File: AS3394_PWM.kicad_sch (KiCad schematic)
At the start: 90 parts, among them U4 LM324, U5 AS3394, U6 LM324

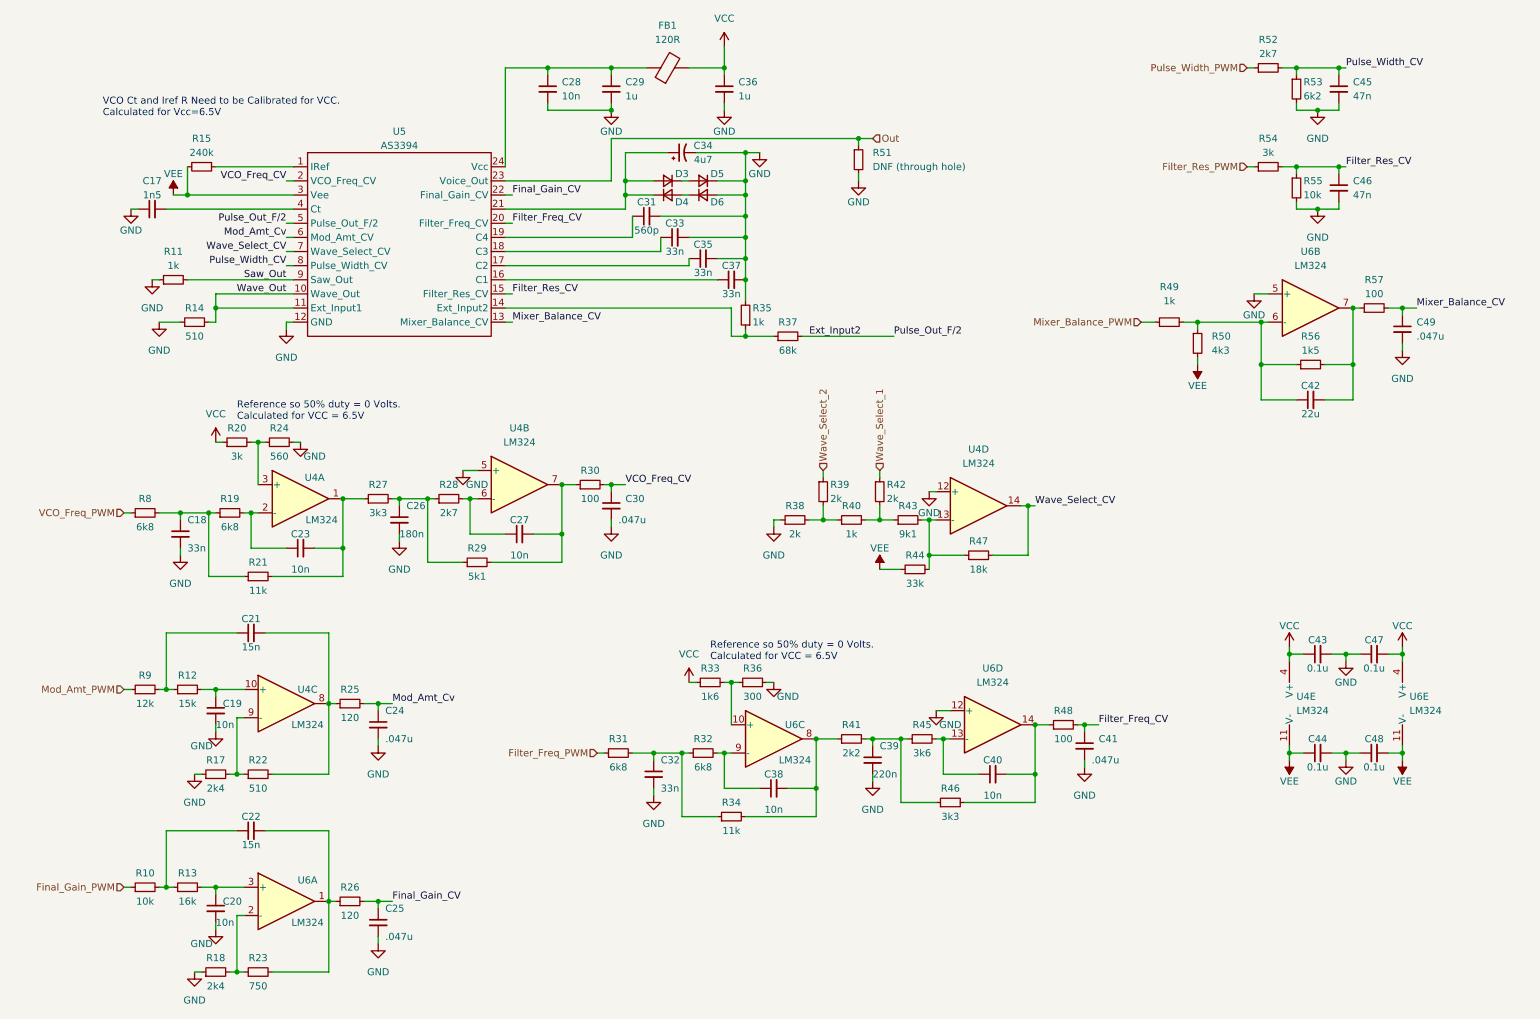
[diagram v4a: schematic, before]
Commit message: Finished most of routing; added TL071 for headphone out; working on adding I/O
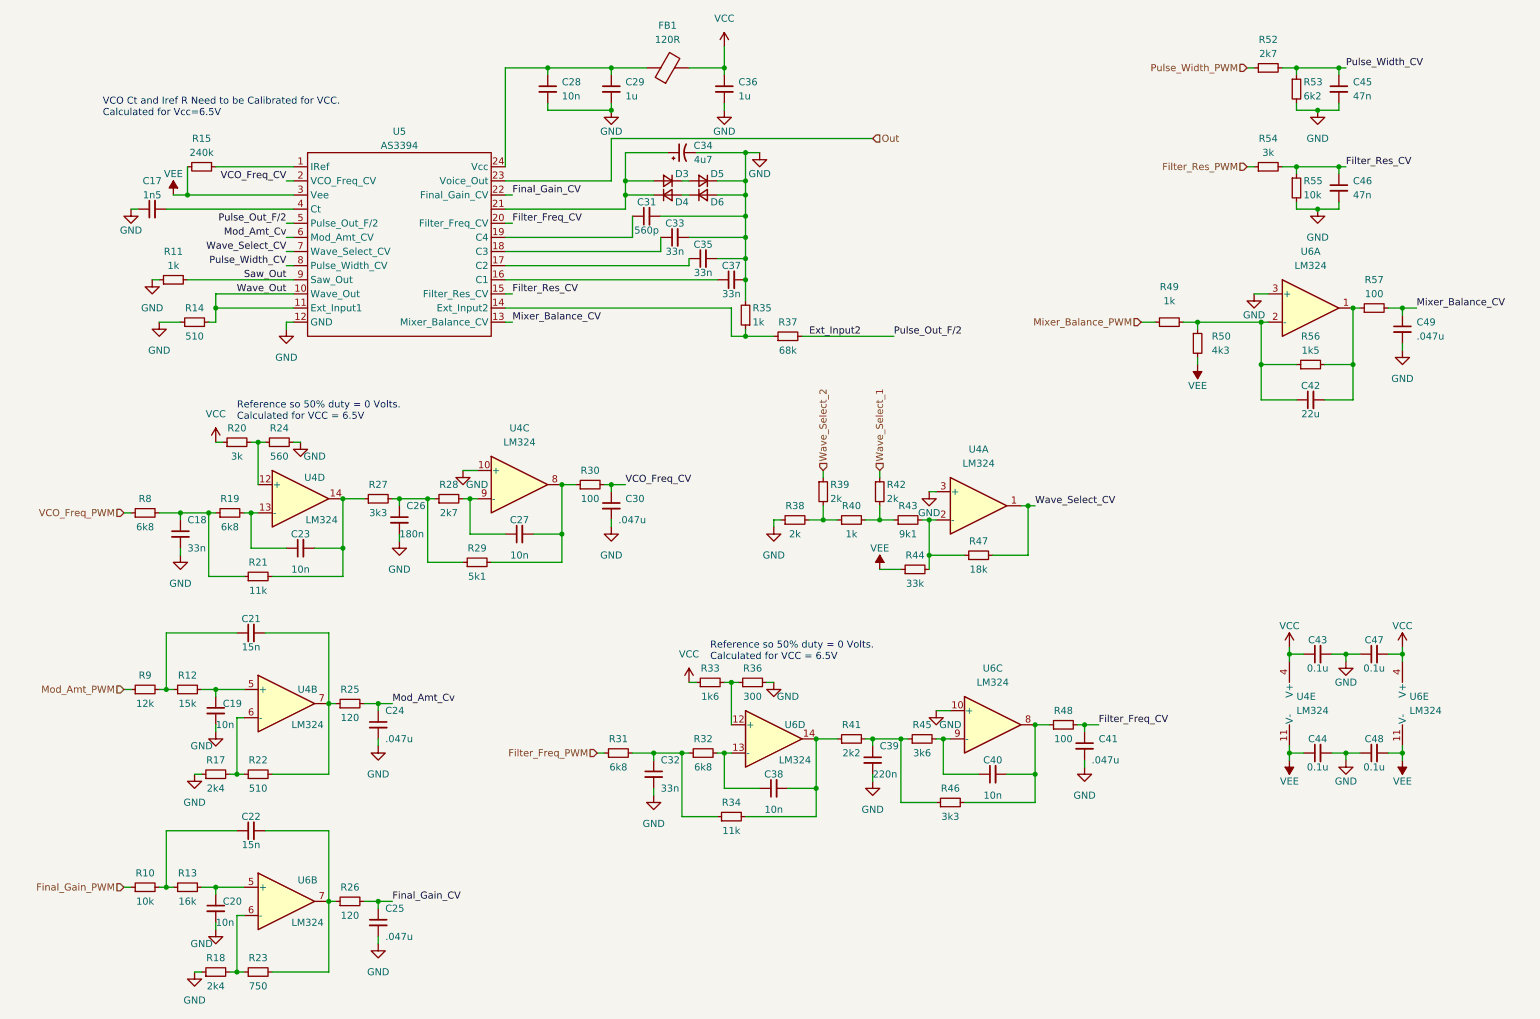
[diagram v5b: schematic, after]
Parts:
- removed R51: DNF (through hole), Resistor_SMD:R_0603_1608Metric, symbol Device:R_Small
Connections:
- net GND: now also U4.10 (+), U4.3 (+), U6.10 (+), U6.3 (+); no longer U4.12 (+), U4.5 (+), U6.12 (+), U6.5 (+)
- net Wave_Select_CV: now also U4.1; no longer U4.14
- net at C21.2, R22.2, R25.1: now also U4.7; no longer U4.8
- net at C19.1, R12.2: now also U4.5 (+); no longer U4.10 (+)
- net at R18.2, R23.1: now also U6.6 (-); no longer U6.2 (-)
- net at C22.2, R23.2, R26.1: now also U6.7; no longer U6.1
- net at R43.2, R44.2, R47.1: now also U4.2 (-); no longer U4.13 (-)
- net at C38.1, R32.2: now also U6.13 (-); no longer U6.9 (-)
- net at C20.1, R13.2: now also U6.5 (+); no longer U6.3 (+)
- net at C23.1, R19.2: now also U4.13 (-); no longer U4.2 (-)
- net at C23.2, R21.2, R27.1: now also U4.14; no longer U4.1
- net at R20.2, R24.1: now also U4.12 (+); no longer U4.3 (+)
- net at C42.1, R49.2, R50.1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: now also U6.2 (-); no longer U6.6 (-)
- net at R17.2, R22.1: now also U4.6 (-); no longer U4.9 (-)
- net at R33.2, R36.1: now also U6.12 (+); no longer U6.10 (+)
- net at C27.1, R28.2: now also U4.9 (-); no longer U4.6 (-)
- net at C40.1, R45.2: now also U6.9 (-); no longer U6.13 (-)
- net at C40.2, R46.2, R48.1: now also U6.8; no longer U6.14
- net at C27.2, R29.2, R30.1: now also U4.8; no longer U4.7
- net at C42.2, R56.2, R57.1: now also U6.1; no longer U6.7
- net at C38.2, R34.2, R41.1: now also U6.14; no longer U6.8
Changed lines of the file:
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@@
   (junction (at 176.53 115.57) (diameter 0) (color 0 0 0 0)
   )
-  (junction (at 163.83 40.64) (diameter 0) (color 0 0 0 0)
-  )
   (junction (at 119.38 35.56) (diameter 0) (color 0 0 0 0)
   )
@@
     (stroke (width 0) (type default) (color 0 0 0 0))
   )
-  (wire (pts (xy 163.83 40.64) (xy 166.37 40.64))
+  (wire (pts (xy 119.38 40.64) (xy 166.37 40.64))
     (stroke (width 0) (type default) (color 0 0 0 0))
   )
@@
     (stroke (width 0) (type default) (color 0 0 0 0))
   )
-  (wire (pts (xy 119.38 40.64) (xy 163.83 40.64))
-    (stroke (width 0) (type default) (color 0 0 0 0))
-  )
   (wire (pts (xy 248.92 133.35) (xy 251.46 133.35))
     (stroke (width 0) (type default) (color 0 0 0 0))
@@
     (stroke (width 0) (type default) (color 0 0 0 0))
   )
-  (wire (pts (xy 163.83 40.64) (xy 163.83 41.91))
-    (stroke (width 0) (type default) (color 0 0 0 0))
-  )
   (wire (pts (xy 166.37 149.86) (xy 166.37 148.59))
     (stroke (width 0) (type default) (color 0 0 0 0))
@@
     (stroke (width 0) (type default) (color 0 0 0 0))
   )
-  (wire (pts (xy 163.83 46.99) (xy 163.83 48.26))
-    (stroke (width 0) (type default) (color 0 0 0 0))
-  )
   (wire (pts (xy 48.26 139.7) (xy 48.26 140.97))
     (stroke (width 0) (type default) (color 0 0 0 0))
@@
     (pin "2")
   )
-  (symbol (lib_id "Amplifier_Operational:LM324") (at 60.96 177.8 0) (unit 1)
+  (symbol (lib_id "Amplifier_Operational:LM324") (at 60.96 177.8 0) (unit 2)
     (in_bom yes) (on_board yes)
     (property "Reference" "U6" (id 0) (at 64.77 173.99 0))
@@
     (pin "1")
   )
-  (symbol (lib_id "Amplifier_Operational:LM324") (at 187.96 146.05 0) (unit 4)
+  (symbol (lib_id "Amplifier_Operational:LM324") (at 187.96 146.05 0) (unit 3)
     (in_bom yes) (on_board yes) (fields_autoplaced)
     (property "Reference" "U6" (id 0) (at 187.96 135.89 0))
@@
     (pin "4")
   )
-  (symbol (lib_id "power:GND") (at 163.83 48.26 0) (unit 1)
-    (in_bom yes) (on_board yes)
-    (property "Reference" "#PWR056" (id 0) (at 163.83 54.61 0)
-      (effects (font (size 1.27 1.27)) hide)
-    )
-    (property "Value" "GND" (id 1) (at 163.83 52.07 0))
-    (property "Footprint" "" (id 2) (at 163.83 48.26 0)
-      (effects (font (size 1.27 1.27)) hide)
-    )
-    (property "Datasheet" "" (id 3) (at 163.83 48.26 0)
-      (effects (font (size 1.27 1.27)) hide)
-    )
-    (pin "1")
-  )
   (symbol (lib_id "power:VCC") (at 133.35 138.43 0) (unit 1)
     (in_bom yes) (on_board yes) (fields_autoplaced)
@@
     (pin "1")
   )
-  (symbol (lib_id "Amplifier_Operational:LM324") (at 102.87 102.87 0) (unit 2)
+  (symbol (lib_id "Amplifier_Operational:LM324") (at 102.87 102.87 0) (unit 3)
     (in_bom yes) (on_board yes) (fields_autoplaced)
     (property "Reference" "U4" (id 0) (at 102.87 92.71 0))
@@
     (pin "2")
   )
-  (symbol (lib_id "Device:R_Small") (at 163.83 44.45 0) (unit 1)
-    (in_bom yes) (on_board yes) (fields_autoplaced)
-    (property "Reference" "R51" (id 0) (at 166.37 43.1799 0)
-      (effects (font (size 1.27 1.27)) (justify left))
-    )
-    (property "Value" "DNF (through hole)" (id 1) (at 166.37 45.7199 0)
-      (effects (font (size 1.27 1.27)) (justify left))
-    )
-    (property "Footprint" "Resistor_SMD:R_0603_1608Metric" (id 2) (at 163.83 44.45 0)
-      (effects (font (size 1.27 1.27)) hide)
-    )
-    (property "Datasheet" "~" (id 3) (at 163.83 44.45 0)
-      (effects (font (size 1.27 1.27)) hide)
-    )
-    (pin "1")
-    (pin "2")
-  )
   (symbol (lib_id "Device:R_Small") (at 237.49 27.94 90) (unit 1)
     (in_bom yes) (on_board yes)
@@
     (pin "2")
   )
-  (symbol (lib_id "Amplifier_Operational:LM324") (at 148.59 148.59 0) (unit 3)
+  (symbol (lib_id "Amplifier_Operational:LM324") (at 148.59 148.59 0) (unit 4)
     (in_bom yes) (on_board yes)
     (property "Reference" "U6" (id 0) (at 152.4 146.05 0))
@@
     (pin "2")
   )
-  (symbol (lib_id "Amplifier_Operational:LM324") (at 63.5 105.41 0) (unit 1)
+  (symbol (lib_id "Amplifier_Operational:LM324") (at 63.5 105.41 0) (unit 4)
     (in_bom yes) (on_board yes)
     (property "Reference" "U4" (id 0) (at 66.04 101.6 0))
@@
     (pin "2")
   )
-  (symbol (lib_id "Amplifier_Operational:LM324") (at 185.42 106.68 0) (unit 4)
+  (symbol (lib_id "Amplifier_Operational:LM324") (at 185.42 106.68 0) (unit 1)
     (in_bom yes) (on_board yes) (fields_autoplaced)
     (property "Reference" "U4" (id 0) (at 185.42 96.52 0))
@@
     (pin "1")
   )
-  (symbol (lib_id "Amplifier_Operational:LM324") (at 245.11 71.12 0) (unit 2)
+  (symbol (lib_id "Amplifier_Operational:LM324") (at 245.11 71.12 0) (unit 1)
     (in_bom yes) (on_board yes) (fields_autoplaced)
     (property "Reference" "U6" (id 0) (at 245.11 60.96 0))
@@
     (pin "4")
   )
-  (symbol (lib_id "Amplifier_Operational:LM324") (at 60.96 142.24 0) (unit 3)
+  (symbol (lib_id "Amplifier_Operational:LM324") (at 60.96 142.24 0) (unit 2)
     (in_bom yes) (on_board yes)
     (property "Reference" "U4" (id 0) (at 64.77 139.7 0))

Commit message: First board prototype ordered from JLC with assembly
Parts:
- C20: footprint Capacitor_SMD:C_01005_0402Metric -> Capacitor_SMD:C_0402_1005Metric
- R20: footprint Resistor_SMD:R_0201_0603Metric -> Resistor_SMD:R_0603_1608Metric
- R44: footprint Resistor_SMD:R_01005_0402Metric -> Resistor_SMD:R_0402_1005Metric
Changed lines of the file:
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@@
     (property "Reference" "R44" (id 0) (at 173.99 115.57 90))
     (property "Value" "33k" (id 1) (at 173.99 120.65 90))
-    (property "Footprint" "Resistor_SMD:R_01005_0402Metric" (id 2) (at 173.99 118.11 0)
+    (property "Footprint" "Resistor_SMD:R_0402_1005Metric" (id 2) (at 173.99 118.11 0)
       (effects (font (size 1.27 1.27)) hide)
     )
@@
     (property "Reference" "R20" (id 0) (at 52.07 92.71 90))
     (property "Value" "3k" (id 1) (at 52.07 97.79 90))
-    (property "Footprint" "Resistor_SMD:R_0201_0603Metric" (id 2) (at 52.07 95.25 0)
+    (property "Footprint" "Resistor_SMD:R_0603_1608Metric" (id 2) (at 52.07 95.25 0)
       (effects (font (size 1.27 1.27)) hide)
     )
@@
       (effects (font (size 1.27 1.27)) (justify left))
     )
-    (property "Footprint" "Capacitor_SMD:C_01005_0402Metric" (id 2) (at 48.26 179.07 0)
-      (effects (font (size 1.27 1.27)) hide)
-    )
+    (property "Footprint" "Capacitor_SMD:C_0402_1005Metric" (id 2) (at 48.26 179.07 0)
+      (effects (font (size 1.27 1.27)) hide)
+    )

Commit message: continuing work on second version
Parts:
- D3, D4, D5, D6: footprint Diode_SMD:D_SMA -> Diode_SMD:D_SOD-123
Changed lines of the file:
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@@
       (effects (font (size 1.27 1.27)) hide)
     )
-    (property "Footprint" "Diode_SMD:D_SMA" (id 2) (at 129.54 50.8 90)
+    (property "Footprint" "Diode_SMD:D_SOD-123" (id 2) (at 129.54 50.8 90)
       (effects (font (size 1.27 1.27)) hide)
     )
@@
       (effects (font (size 1.27 1.27)) hide)
     )
-    (property "Footprint" "Diode_SMD:D_SMA" (id 2) (at 135.89 48.26 90)
+    (property "Footprint" "Diode_SMD:D_SOD-123" (id 2) (at 135.89 48.26 90)
       (effects (font (size 1.27 1.27)) hide)
     )
@@
       (effects (font (size 1.27 1.27)) hide)
     )
-    (property "Footprint" "Diode_SMD:D_SMA" (id 2) (at 129.54 48.26 90)
+    (property "Footprint" "Diode_SMD:D_SOD-123" (id 2) (at 129.54 48.26 90)
       (effects (font (size 1.27 1.27)) hide)
     )
@@
       (effects (font (size 1.27 1.27)) hide)
     )
-    (property "Footprint" "Diode_SMD:D_SMA" (id 2) (at 135.89 57.15 90)
-      (effects (font (size 1.27 1.27)) hide)
-    )
+    (property "Footprint" "Diode_SMD:D_SOD-123" (id 2) (at 135.89 57.15 90)
+      (effects (font (size 1.27 1.27)) hide)
+    )

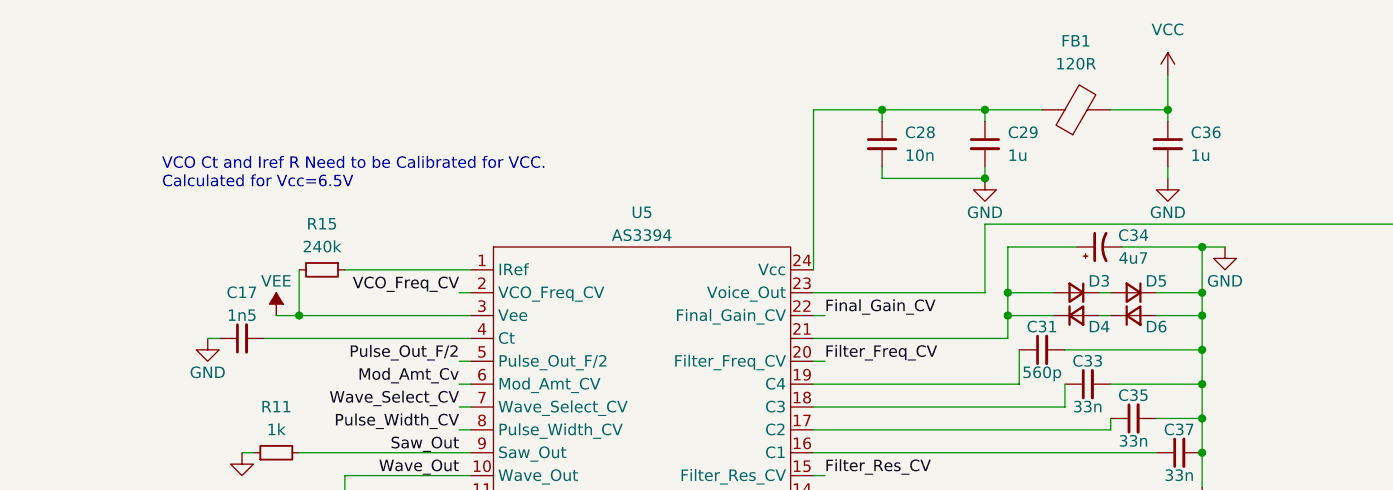
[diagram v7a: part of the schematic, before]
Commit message: added separate LDO for 3394, removed amp, designed psu board and made project for carrier board
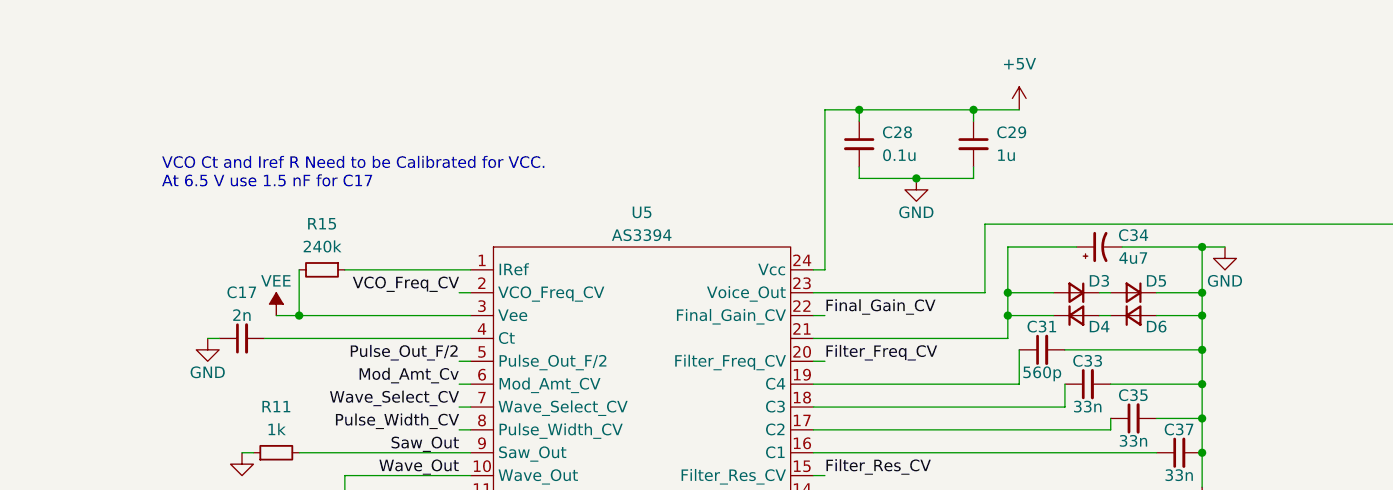
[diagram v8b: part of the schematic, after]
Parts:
- removed C36: 1u, Capacitor_SMD:C_0402_1005Metric, symbol Device:C_Small
- removed FB1: 120R, Inductor_SMD:L_0805_2012Metric, symbol Device:FerriteBead
- C17: value 1n5 -> 2n
- C28: value 10n -> 0.1u
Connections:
- net +5V: now reaches C28.1, C29.1, U5.24 (Vcc)
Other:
- note added: "VCO Ct and Iref R Need to be Calibrated for VCC. At 6.5 V use 1.5 nF for C17"
- note removed: "VCO Ct and Iref R Need to be Calibrated for VCC. Calculated for Vcc=6.5V"
- moved on the sheet: C28, C29
